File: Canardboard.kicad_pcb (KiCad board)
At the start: 4 copper layers, 125 parts, among them IC1 SIC437DED-T1-GE3, J1 RBUS, J2 USB_C_Receptacle_USB2.0, J3 Micro_SD_Card_Det, J4 Conn_01x02_Male, J5 Conn_01x03_Male, J6 Conn_01x03_Male, J7 Conn_01x03_Male, Q1 SI4143DY-T1-GE3, Q2 SI4143DY-T1-GE3, U1 ESP32-S3, U2 SN65HVD230, U3 LM66200DRLR, U4 LTC4412xS6, U5 MAX77827AEFD+T, U6 SC4215, U7 ICM-20608-G, U8 MMC5983MA, U9 LTC4412xS6, Y1 40MHz±10ppm

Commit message: first draft of PCB layout
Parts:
- J1: footprint Connector_Molex:Molex_Mini-Fit_Jr_5566-06A_2x03_P4.20mm_Vertical -> Connector_Molex:Molex_Mini-Fit_Jr_5569-06A2_2x03_P4.20mm_Horizontal
- moved H3 253.8 mm to (39.5, 153.6)
- moved H1 236.5 mm to (38.5, 85.1)
- moved H4 218.4 mm to (75.5, 153.6)
- moved TP7 215.5 mm to (38.0, 117.6)
- moved TP5 213.5 mm to (38.0, 128.6)
- moved TP4 211.7 mm to (40.5, 117.6)
- moved TP6 211.3 mm to (40.5, 128.6)
- moved TP8 211.2 mm to (43.0, 117.6)
- moved H2 201.8 mm to (72.5, 85.1)
- moved R17 174.9 mm to (57.0, 124.6), turned to 90 degrees
- moved R18 174.4 mm to (55.0, 120.1), turned to -90 degrees
- moved R22 173.3 mm to (54.5, 121.6), turned to 180 degrees
- moved R20 170.8 mm to (59.0, 124.6), turned to -90 degrees
- moved R19 170.7 mm to (60.0, 124.6), turned to -90 degrees
- moved C29 170.4 mm to (61.2, 103.9), turned to 180 degrees
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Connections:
- C39 pad 1: Net-(C39-Pad1) -> GND
- C39 pad 2: /servopower/VIN -> +12V
- C40 pad 2: /servopower/VIN -> +12V
- C45 pad 1: Net-(C39-Pad1) -> GND
- C45 pad 2: /servopower/VIN -> +12V
- C46 pad 1: Net-(C39-Pad1) -> GND
- C46 pad 2: /servopower/VIN -> +12V
- IC1 pad 1: /servopower/VIN -> +12V
- IC1 pad 19: /servopower/VIN -> +12V
- IC1 pad 2: /servopower/VIN -> +12V
- IC1 pad 22: /servopower/VIN -> +12V
- IC1 pad 26: /servopower/VIN -> +12V
- J1 pad 4: +12V -> /RBUS_DEPL
- Q2 pad 1: /RBUS_PWR -> /RBUS_DEPL
- Q2 pad 2: /RBUS_PWR -> /RBUS_DEPL
- Q2 pad 3: /RBUS_PWR -> /RBUS_DEPL
- U9 pad 1: /RBUS_PWR -> /RBUS_DEPL
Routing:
- net (no net): track 0.00 -> 0.75 mm
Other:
- board outline added: 47 x 77.5 mm

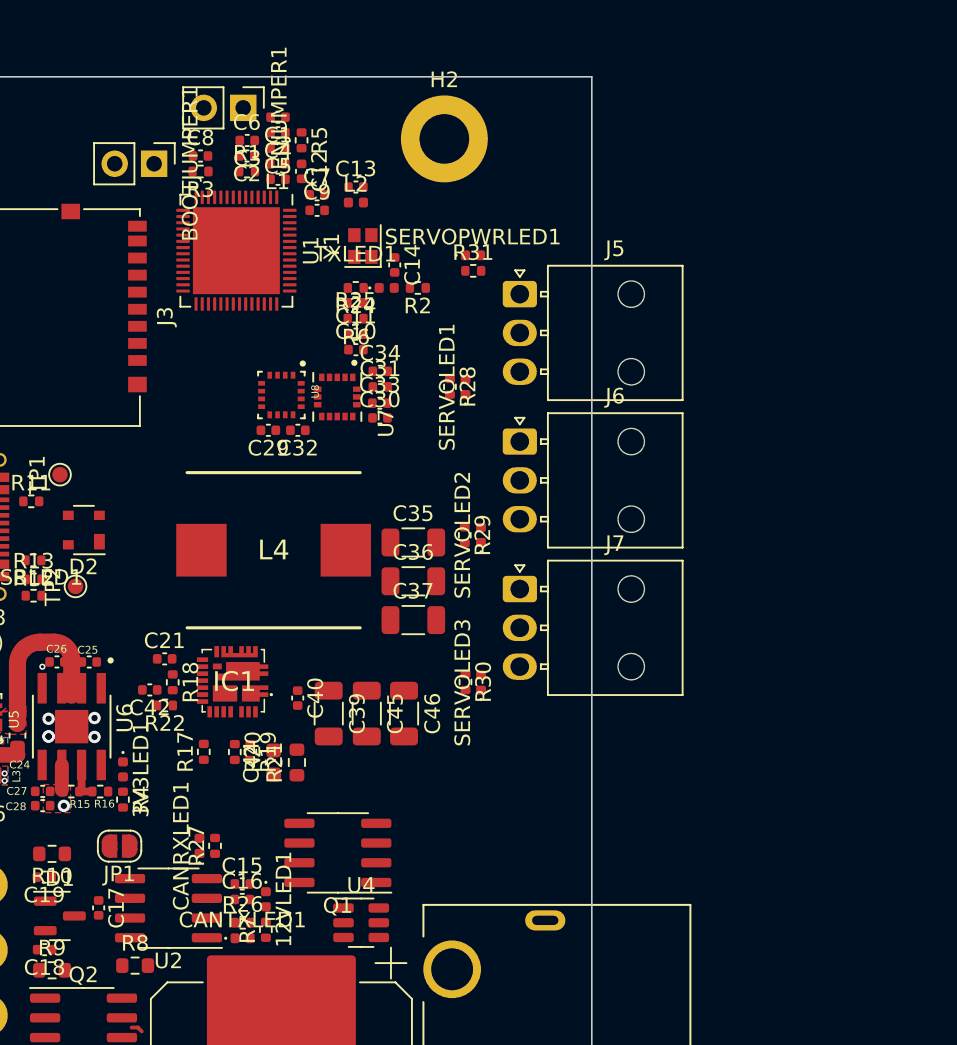
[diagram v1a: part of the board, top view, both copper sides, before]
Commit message: error encountered - battery logic and inductor
- use large capacitor?
- use VBUS as a power source?
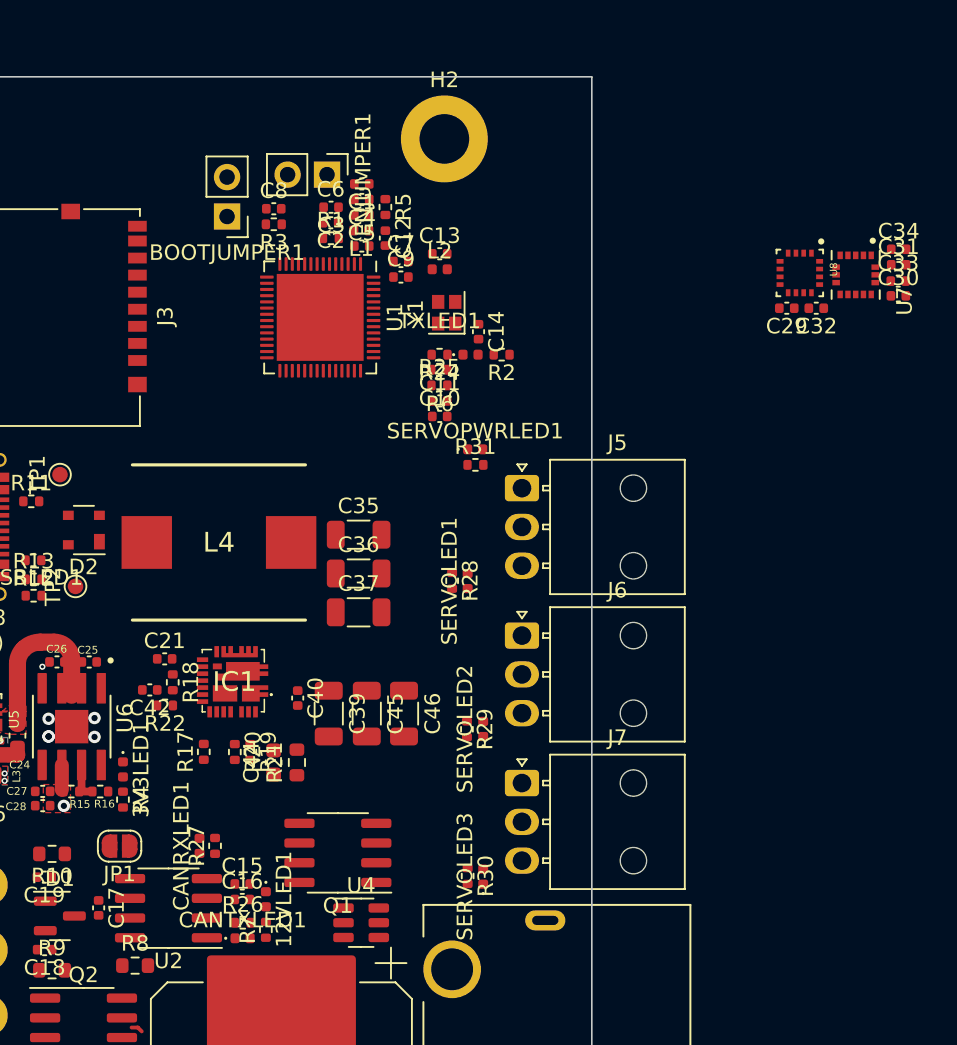
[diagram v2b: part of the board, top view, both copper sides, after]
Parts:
- moved C29 34.3 mm to (94.6, 96.0)
- moved C30 34.3 mm to (101.8, 95.2)
- moved U7 34.3 mm to (99.0, 93.8)
- moved U8 34.3 mm to (95.4, 93.7)
- moved C31 34.3 mm to (101.8, 93.2)
- moved C32 34.3 mm to (96.5, 96.0)
- moved C33 34.3 mm to (101.7, 94.2)
- moved C34 34.3 mm to (101.8, 92.2)
- moved R30 12.5 mm to (74.0, 132.6)
- moved J5 12.5 mm to (77.5, 107.6)
- moved J6 12.5 mm to (77.5, 117.1)
- moved J7 12.5 mm to (77.5, 126.6)
- moved R28 12.5 mm to (73.0, 113.6)
- moved R29 12.5 mm to (74.0, 123.1)
- moved R31 12.5 mm to (74.5, 106.1)
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
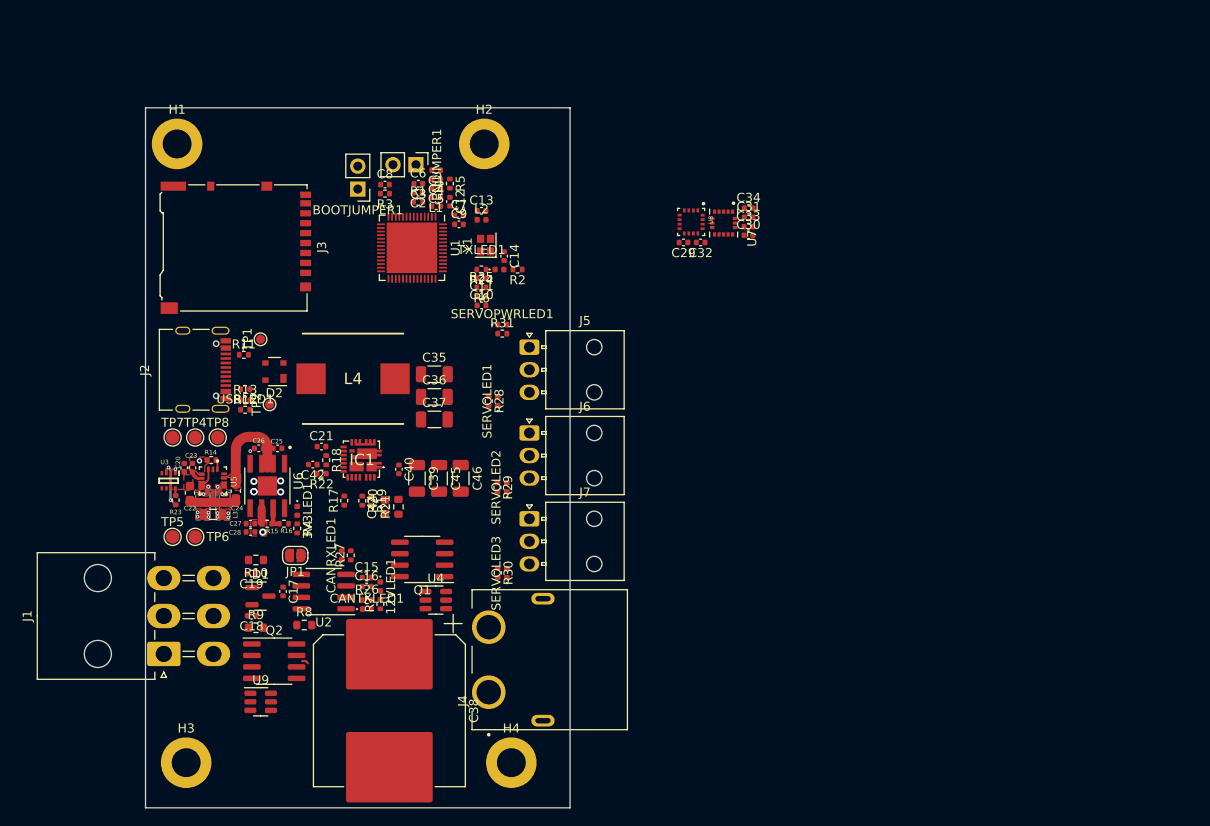
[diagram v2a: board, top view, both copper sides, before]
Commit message: power draft 2, power fixed I think
10 mosfets now!

2 each on:

Servo power: 3s/4s LIPO, RBUS_DEPL
3.3: VBUS, RBUS_3.3, 3s/4s LIPO

fixed some capacitors
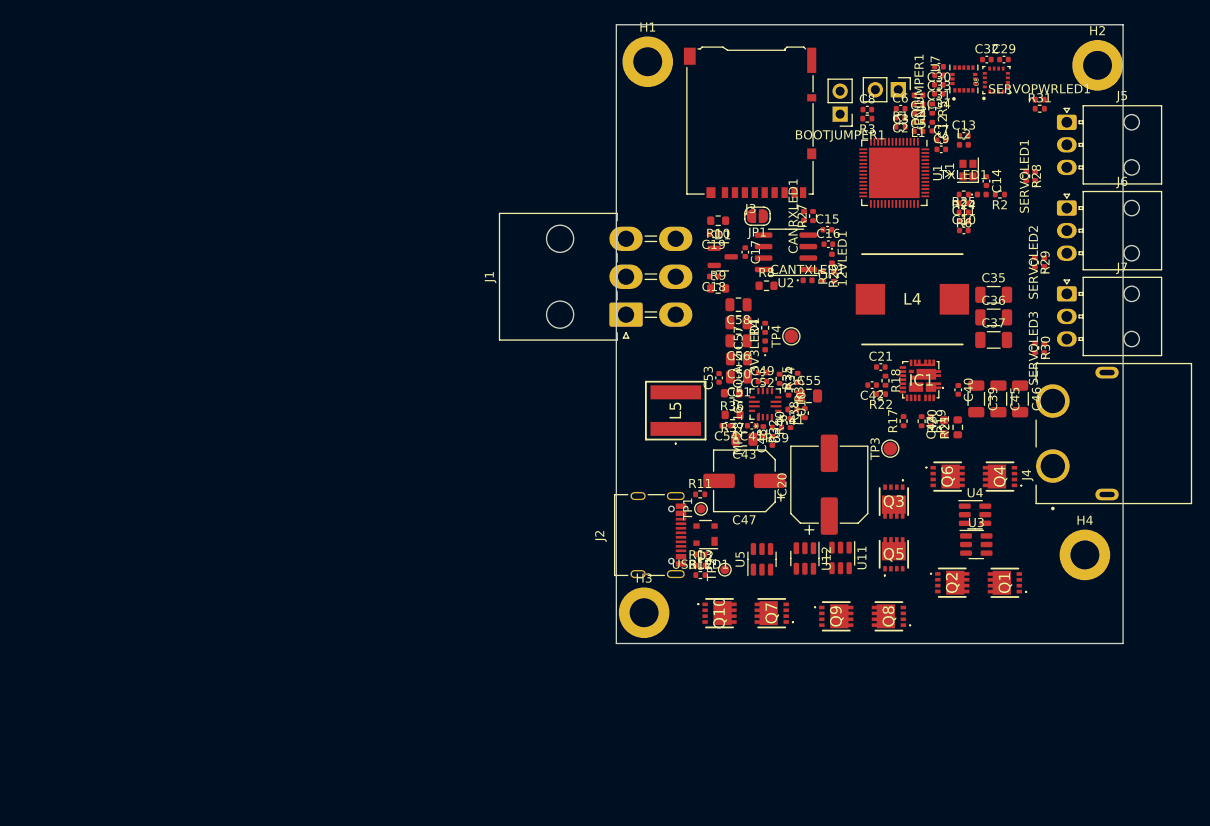
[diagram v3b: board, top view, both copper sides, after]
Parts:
- removed C22: 10uF, Capacitor_SMD:C_0603_1608Metric
- removed C23: 1uF, Capacitor_SMD:C_0402_1005Metric
- removed C24: 22uF, Capacitor_SMD:C_0603_1608Metric
- removed C25, C27: 10uF, Capacitor_SMD:C_0402_1005Metric
- removed C26: 4.7uF, Capacitor_SMD:C_0402_1005Metric
- removed C28: 0.1uF, Capacitor_SMD:C_0402_1005Metric
- removed C38: 2200uF, Capacitor_SMD:CP_Elec_16x17.5
- removed L3: 1uH, Inductor_SMD:L_0805_2012Metric
- removed R14: 14k, Resistor_SMD:R_0402_1005Metric
- removed R15: 56k, Resistor_SMD:R_0402_1005Metric
- removed R16, R23: 10k, Resistor_SMD:R_0402_1005Metric
- removed TP5, TP6, TP7, TP8: TestPoint, TestPoint:TestPoint_Pad_D1.5mm
- removed U6: SC4215, iclr:SOIC127P599X175-9N
- removed U9: LTC4412xS6, Package_TO_SOT_SMD:TSOT-23-6
- added C41: 100nF, Capacitor_SMD:C_0402_1005Metric, F.Cu at (102.1, 116.3)
- added C43: 22uF, Capacitor_SMD:C_0805_2012Metric, F.Cu at (101.3, 117.8)
- added C47: 100uF, Capacitor_SMD:CP_Elec_6.3x5.4, F.Cu at (101.3, 122.4)
- added C48: 22nF, Capacitor_SMD:C_0402_1005Metric, F.Cu at (104.4, 118.0)
- added C49: 100nF, Capacitor_SMD:C_0402_1005Metric, F.Cu at (103.3, 111.4)
- added C50: 22uF, Capacitor_SMD:C_0805_2012Metric, F.Cu at (100.7, 108.9)
- added C51: 22uF, Capacitor_SMD:C_0805_2012Metric, F.Cu at (100.7, 110.9)
- added C52: 1uF, Capacitor_SMD:C_0402_1005Metric, F.Cu at (103.3, 110.4)
- added C53: 100nF, Capacitor_SMD:C_0402_1005Metric, F.Cu at (98.5, 111.0)
- added C54: 100nF, Capacitor_SMD:C_0402_1005Metric, F.Cu at (99.3, 116.3)
- added C55: 22nF, Capacitor_SMD:C_0805_2012Metric, F.Cu at (108.5, 113.0)
- added C56: 22uF, Capacitor_SMD:C_0805_2012Metric, F.Cu at (100.7, 106.9)
- added C57: 22uF, Capacitor_SMD:C_0805_2012Metric, F.Cu at (100.7, 104.9)
- added C58: 22uF, Capacitor_SMD:C_0805_2012Metric, F.Cu at (100.7, 102.9)
- added L5: 4.7uH, iclr:MPLAL60504R7, F.Cu at (93.7, 114.6)
- added Q10: PXP012-30QLJ, iclr:PXP01230QLJ, F.Cu at (98.5, 137.0)
- added Q3: PXP012-30QLJ, iclr:PXP01230QLJ, F.Cu at (117.8, 124.7)
- added Q4: PXP012-30QLJ, iclr:PXP01230QLJ, F.Cu at (129.6, 121.9)
- added Q5: PXP012-30QLJ, iclr:PXP01230QLJ, F.Cu at (117.8, 130.5)
- added Q6: PXP012-30QLJ, iclr:PXP01230QLJ, F.Cu at (123.8, 121.9)
- added Q7: PXP012-30QLJ, iclr:PXP01230QLJ, F.Cu at (104.3, 137.0)
- added Q8: PXP012-30QLJ, iclr:PXP01230QLJ, F.Cu at (117.3, 137.4)
- added Q9: PXP012-30QLJ, iclr:PXP01230QLJ, F.Cu at (111.5, 137.4)
- added R32: 499k, Resistor_SMD:R_0402_1005Metric, F.Cu at (103.4, 116.9)
- added R33: 806k, Resistor_SMD:R_0402_1005Metric, F.Cu at (106.2, 112.4)
- added R34: 230k, Resistor_SMD:R_0402_1005Metric, F.Cu at (105.2, 111.1)
- added R35: 100k, Resistor_SMD:R_0402_1005Metric, F.Cu at (107.2, 111.0)
- added R36: 0, Resistor_SMD:R_0603_1608Metric, F.Cu at (99.9, 112.7)
- added R37: 0, Resistor_SMD:R_0603_1608Metric, F.Cu at (100.0, 115.1)
- added R38: 21.5k, Resistor_SMD:R_0402_1005Metric, F.Cu at (108.0, 114.9)
- added R39: 10k, Resistor_SMD:R_0402_1005Metric, F.Cu at (104.9, 116.5)
- added R40: 10k, Resistor_SMD:R_0402_1005Metric, F.Cu at (106.4, 116.0)
- added R41: 10k, Resistor_SMD:R_0402_1005Metric, F.Cu at (106.6, 114.5)
- added TP3: TestPoint, TestPoint:TestPoint_Pad_D1.5mm, F.Cu at (117.5, 118.8)
- added U10: MP28167GQ-A-Z, iclr:MP28167GQ-A-Z, F.Cu at (103.6, 113.9)
- added U11: LTC4412xS6, Package_TO_SOT_SMD:TSOT-23-6, F.Cu at (112.0, 130.9)
- added U12: LTC4412xS6, Package_TO_SOT_SMD:TSOT-23-6, F.Cu at (108.0, 131.0)
- C20: value 10uF -> 390uF; footprint Capacitor_SMD:C_0402_1005Metric -> Capacitor_SMD:CP_Elec_8x11.9
- Q1, Q2: value SI4143DY-T1-GE3 -> PXP012-30QLJ; footprint Package_SO:SOIC-8_3.9x4.9mm_P1.27mm -> iclr:PXP01230QLJ
- U3: value LM66200DRLR -> LTC4412xS6; footprint iclr:SOTFL50P160X60-8N -> Package_TO_SOT_SMD:TSOT-23-6
- U5: value MAX77827AEFD+T -> LTC4412xS6; footprint iclr:CONV_MAX77827AEFD+T -> Package_TO_SOT_SMD:TSOT-23-6
- moved U3 89.7 mm to (127.0, 129.4), turned to 0 degrees
- moved Q2 75.6 mm to (124.3, 133.7), turned to -90 degrees
- moved C20 71.4 mm to (110.7, 122.8)
- moved H2 68.5 mm to (140.4, 76.4)
- moved H4 67.5 mm to (139.0, 130.6)
- moved J4 67.3 mm to (135.4, 117.2)
- moved TP4 66.9 mm to (106.5, 106.4), turned to 90 degrees
- moved Q1 64.6 mm to (130.1, 133.7), turned to 90 degrees
- moved R29 64.5 mm to (133.5, 98.2)
- moved SERVOPWRLED1 64.5 mm to (134.0, 80.2)
- moved J5 64.5 mm to (137.0, 82.7)
- moved J6 64.5 mm to (137.0, 92.2)
- moved J7 64.5 mm to (137.0, 101.7)
- moved R28 64.5 mm to (132.5, 88.7)
- moved R30 64.5 mm to (133.5, 107.7)
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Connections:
- C20 pad 1: /Power/BBIN -> RBUS_uC_V
- J1 pad 3: RBUS_uC_V -> VBUS
- J1 pad 4: /RBUS_DEPL -> /rbusmosfets/RBUS_DEPL
- J4 pad 1: Net-(J4-Pin_1) -> /rbusmosfets/BatteryPower
- Q1 pad 1: Net-(J4-Pin_1) -> Net-(Q1-S_1)
- Q1 pad 2: Net-(J4-Pin_1) -> Net-(Q1-S_1)
- Q1 pad 3: Net-(J4-Pin_1) -> Net-(Q1-S_1)
- Q1 pad 5: +12V -> Net-(Q1-D_1)
- Q1 pad 6: +12V -> Net-(Q1-D_1)
- Q1 pad 7: +12V -> Net-(Q1-D_1)
- Q1 pad 8: +12V -> Net-(Q1-D_1)
- Q2 pad 1: /RBUS_DEPL -> +12V
- Q2 pad 2: /RBUS_DEPL -> +12V
- Q2 pad 3: /RBUS_DEPL -> +12V
- Q2 pad 4: Net-(Q2-G) -> Net-(Q1-G)
- Q2 pad 5: +12V -> Net-(Q1-D_1)
- Q2 pad 6: +12V -> Net-(Q1-D_1)
- Q2 pad 7: +12V -> Net-(Q1-D_1)
- Q2 pad 8: +12V -> Net-(Q1-D_1)
- TP4 pad 1: /Power/BBIN -> +3V3
- U3 pad 1: GND -> Net-(Q1-S_1)
- U3 pad 2: /Power/BBIN -> GND
- U3 pad 3: VBUS -> /rbusmosfets/BatteryPower
- U3 pad 4: GND -> unconnected-(U3-STAT-Pad4)
- U3 pad 5: GND -> Net-(Q1-G)
- U3 pad 6: RBUS_uC_V -> +12V
- U4 pad 1: Net-(J4-Pin_1) -> /rbusmosfets/BatteryPower
- U4 pad 5: Net-(Q1-G) -> Net-(Q4-G)
- U5 pad 1: /Power/SEL -> VBUS
- U5 pad 2: unconnected-(U5-POK-Pad2) -> GND
- U5 pad 3: /Power/BBIN -> GND
- U5 pad 4: GND -> unconnected-(U5-STAT-Pad4)
- U5 pad 5: /Power/BIAS -> Net-(Q10-G)
- U5 pad 6: /Power/BBIN -> Net-(Q7-S_1)
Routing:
- net /Power/BBOUT: track 12.3 -> 0.00 mm
- net GND: track 6.73 -> 0.00 mm, vias 6 -> 0
- net VBUS: track 5.27 -> 0.00 mm, vias 2 -> 0
- net /Power/BBIN: track 3.68 -> 0.00 mm, vias 2 -> 0
- net /Power/FBIn: track 2.61 -> 0.00 mm
- net +3V3: track 1.61 -> 0.00 mm, vias 1 -> 0
- net /Power/BIAS: track 1.42 -> 0.00 mm
- net /Power/SEL: track 1.01 -> 0.00 mm
- net Net-(U3-ST): track 0.81 -> 0.00 mm
- net (no net): track 0.75 -> 0.00 mm
- net /Power/LX2: vias 7 -> 0
- net /Power/LX1: vias 7 -> 0
- removed copper zone on F.Cu, net +3V3
- removed copper zone on F.Cu, net /Power/BBIN
- removed copper zone on F.Cu, net /Power/BBOUT
- removed copper zone on B.Cu, net /Power/LX1
- removed copper zone on F.Cu, net /Power/LX1
- removed copper zone on B.Cu, net /Power/LX2
- removed copper zone on F.Cu, net /Power/LX2
- removed copper zone on F.Cu, net GND
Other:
- board size 47 x 77.5 mm -> 56.1 x 68.5 mm

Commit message: PCB layout work
pcb layout work
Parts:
- moved Q3 27.2 mm to (126.2, 150.6)
- moved Q10 27.2 mm to (107.0, 162.9)
- moved Q5 27.2 mm to (126.2, 156.4)
- moved Q8 27.2 mm to (125.7, 163.3)
- moved Q9 27.2 mm to (119.9, 163.3)
- moved U12 27.2 mm to (116.4, 156.9)
- moved U5 27.2 mm to (111.7, 157.0)
- moved C20 27.2 mm to (119.1, 148.7)
- moved Q7 27.2 mm to (112.7, 162.9)
- moved TP3 27.2 mm to (125.8, 144.7)
- moved U11 27.2 mm to (120.3, 156.8)
- moved R17 20.0 mm to (130.6, 99.6), turned to 180 degrees
- moved R22 19.6 mm to (131.7, 100.6), turned to 0 degrees
- moved C42 19.3 mm to (132.1, 102.0), turned to 90 degrees
- moved R20 16.7 mm to (129.0, 101.2), turned to 90 degrees
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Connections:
- BOOTJUMPER1 pad 1: /BOOT -> unconnected-(BOOTJUMPER1-Pin_1-Pad1)
- BOOTJUMPER1 pad 2: GND -> /BOOT
- U1 pad 38: /SPI_CLK -> /SD_CS
- U1 pad 39: /SPI_MOSI -> /SPI_CLK
- U1 pad 40: /SPI_MISO -> /SPI_MOSI
- U1 pad 41: /IMU_CS -> /SPI_MISO
- U1 pad 42: /MAG_CS -> /SERVO_SGNL2
- U1 pad 43: /SD_CS -> /SERVO_SGNL1
- U1 pad 44: /SERVO_SGNL1 -> /SERVO_SGNL3
- U1 pad 45: /SERVO_SGNL2 -> /IMU_CS
- U1 pad 47: /SERVO_SGNL3 -> /MAG_CS
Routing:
- net +12V: track 0.00 -> 20.4 mm
- net Net-(Q4-G): track 0.00 -> 18.3 mm
- net +3V3: track 0.00 -> 9.69 mm, vias 0 -> 2
- net /servopower/VDD: track 0.00 -> 9.62 mm, vias 0 -> 2
- net /rbusmosfets/BatteryPower: track 0.00 -> 7.48 mm
- net Net-(U1-XTAL_N): track 0.00 -> 6.50 mm
- net /CHIP_PU: track 0.00 -> 5.90 mm
- net Net-(IC1-FB): track 0.00 -> 4.96 mm
- net Net-(U1-U0TXD/PROG/GPIO43): track 0.00 -> 4.81 mm
- net GNDA: track 0.00 -> 4.45 mm
- net /BuckPGOOD: track 0.00 -> 4.04 mm
- net /BOOT: track 0.00 -> 3.41 mm
- net Net-(C14-Pad1): track 0.00 -> 3.01 mm
- net Net-(IC1-PHASE): track 0.00 -> 2.60 mm
- net Net-(Q4-D_1): track 0.00 -> 2.59 mm
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- added copper zone on In2.Cu, net +3V3
- added copper zone on In1.Cu, net GND
